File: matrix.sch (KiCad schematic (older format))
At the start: 94 parts, among them SW11 SW_Push, SW12 SW_Push, SW13 SW_Push, SW14 SW_Push, SW16 SW_Push, SW17 SW_Push, SW18 SW_Push, SW2 SW_Push, SW20 SW_Push, SW21 SW_Push, SW22 SW_Push, SW23 SW_Push, SW25 SW_Push, SW26 SW_Push, SW27 SW_Push, SW28 SW_Push, SW3 SW_Push, SW30 SW_Push, SW31 SW_Push, SW32 SW_Push, SW34 SW_Push, SW35 SW_Push, SW36 SW_Push, SW37 SW_Push, SW39 SW_Push, SW4 SW_Push, SW40 SW_Push, SW41 SW_Push, SW43 SW_Push, SW44 SW_Push, SW45 SW_Push, SW46 SW_Push, SW48 SW_Push, SW49 SW_Push, SW5 SW_Push, SW50 SW_Push, SW52 SW_Push, SW53 SW_Push, SW54 SW_Push, SW56 SW_Push, SW57 SW_Push, SW58 SW_Push, SW61 SW_Push, SW62 SW_Push, SW7 SW_Push, SW8 SW_Push, SW9 SW_Push

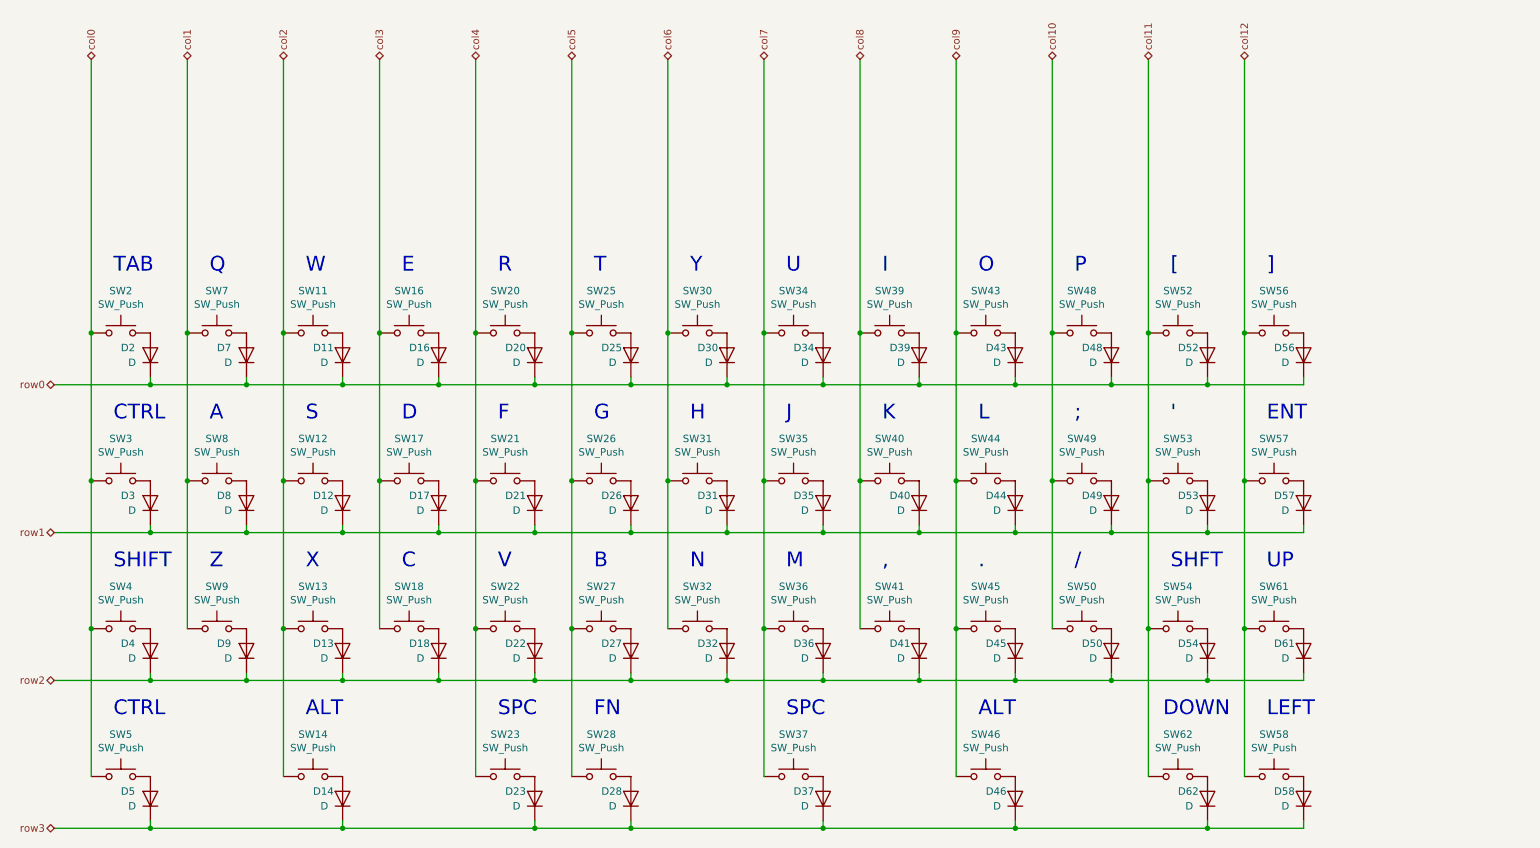
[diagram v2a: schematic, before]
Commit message: Make 69 spacebar layout lol.
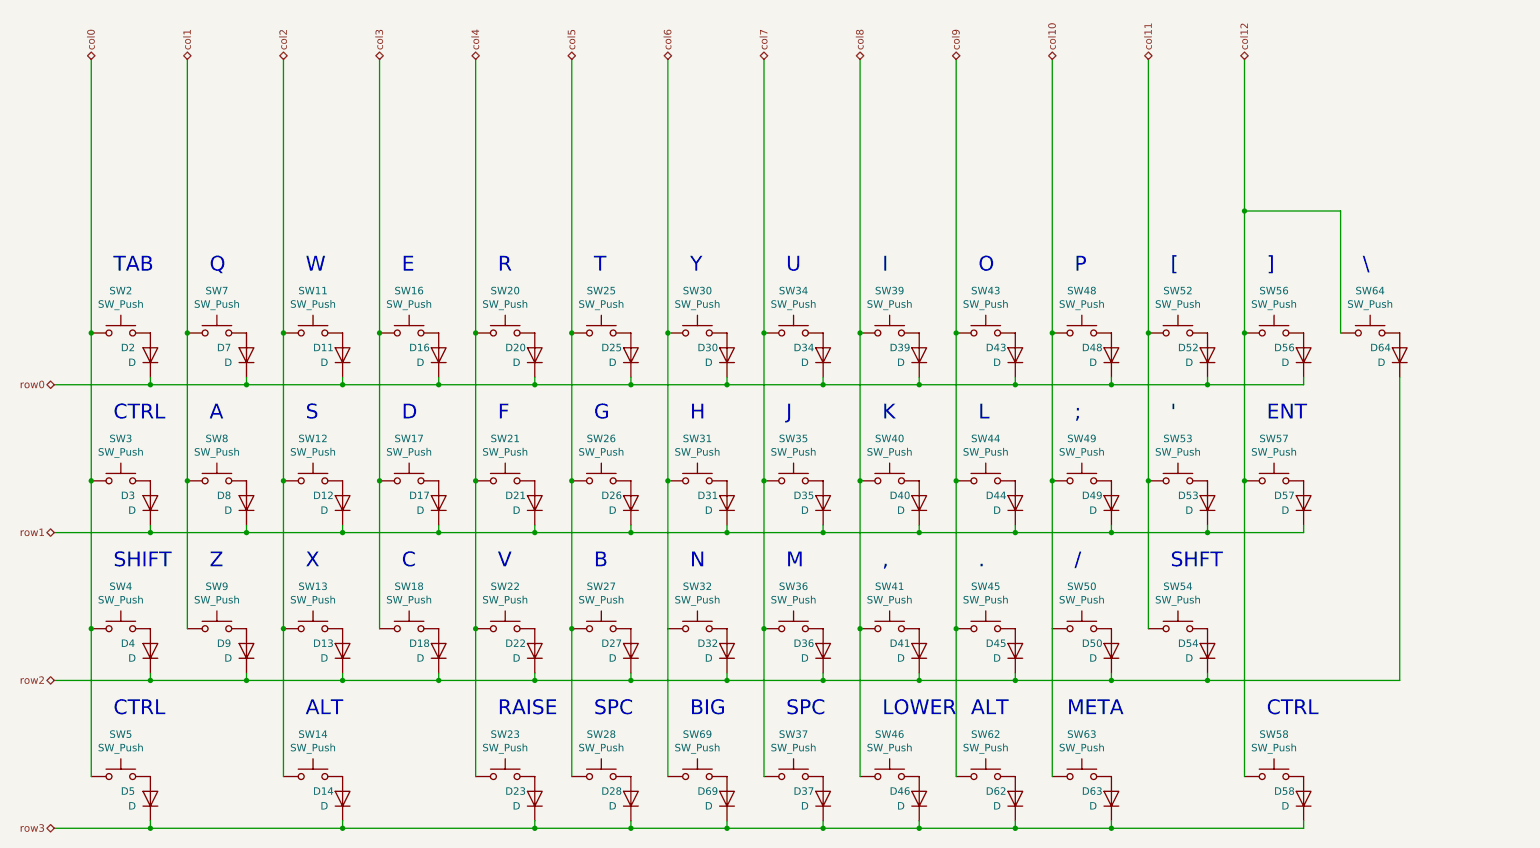
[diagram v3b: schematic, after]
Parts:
- removed D61: D, Diodes_SMD:D_SOD-123, symbol Device:D
- removed SW61: SW_Push, Fate_Parts:SW_Cherry_MX_1.00u_PCB, symbol Switch:SW_Push
- added D63, D64, D69: D, Diode_SMD:D_SOD-123, symbol Device:D
- added SW63, SW64: SW_Push, MX_Switch:SW_Cherry_MX_1.00u_PCB, symbol Switch:SW_Push
- added SW69: SW_Push, Button_Switch_Keyboard:SW_Cherry_MX_6.25u_PCB, symbol Switch:SW_Push
- SW11, SW12, SW13, SW16, SW17, SW18, SW20, SW21, SW22, SW25, SW26, SW27, SW30, SW31, SW32, SW34, SW35, SW36, SW39, SW40, SW41, SW43, SW44, SW45, SW48, SW49, SW50, SW52, SW53, SW56, SW7, SW8, SW9: footprint Fate_Parts:SW_Cherry_MX_1.00u_PCB -> MX_Switch:SW_Cherry_MX_1.00u_PCB
- SW14, SW2, SW46, SW5: footprint Fate_Parts:SW_Cherry_MX_1.50u_PCB -> MX_Switch:SW_Cherry_MX_1.50u_PCB
- SW23: footprint Fate_Parts:SW_Cherry_MX_2.00u_PCB_ReversedStabilizers -> MX_Switch:SW_Cherry_MX_1.00u_PCB
- SW28: footprint Fate_Parts:SW_Cherry_MX_1.00u_PCB -> MX_Switch:SW_Cherry_MX_2.25u_PCB_ReversedStabilizers
- SW3: footprint Fate_Parts:SW_Cherry_MX_1.75u_PCB -> MX_Switch:SW_Cherry_MX_1.75u_PCB
- SW37: footprint Fate_Parts:SW_Cherry_MX_2.75u_PCB_ReversedStabilizers -> MX_Switch:SW_Cherry_MX_2.25u_PCB_ReversedStabilizers
- SW4: footprint Fate_Parts:SW_Cherry_MX_2.25u_PCB -> MX_Switch:SW_Cherry_MX_2.25u_PCB
- SW54: footprint Fate_Parts:SW_Cherry_MX_1.75u_PCB -> MX_Switch:SW_Cherry_MX_2.75u_PCB
- SW57: footprint Fate_Parts:SW_Cherry_MX_2.25u_PCB_ReversedStabilizers -> MX_Switch:SW_Cherry_MX_2.25u_PCB_ReversedStabilizers
- SW58, SW62: footprint Fate_Parts:SW_Cherry_MX_1.00u_PCB -> MX_Switch:SW_Cherry_MX_1.50u_PCB
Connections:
- net col10: now also SW63.1
- net col11: no longer SW62.1
- net col12: now also SW64.1
- net col6: now also SW69.1
- net col8: now also SW46.1
- net col9: now also SW62.1; no longer SW46.1
- net row2: now also D64.1 (K)
- net row3: now also D63.1 (K), D69.1 (K)
- new net: D69.2 (A), SW69.2
- new net: D63.2 (A), SW63.2
- new net: D64.2 (A), SW64.2
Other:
- note added: "BIG"
- note added: "LOWER"
- note added: "META"
- note added: "RAISE"
- note added: "\"
- note removed: "DOWN"
- note removed: "FN"
- note removed: "LEFT"
- note removed: "UP"
- moved on the sheet: D46, D62, SW46, SW62

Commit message: Make it even MORE symmetrical!
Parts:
- removed D69: D, Diode_SMD:D_SOD-123, symbol Device:D
- removed SW69: SW_Push, Button_Switch_Keyboard:SW_Cherry_MX_6.25u_PCB, symbol Switch:SW_Push
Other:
- note removed: "BIG"
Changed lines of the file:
@@
 CTRL
-Wire Wire Line
-	4850 5950 5500 5950
 Wire Wire Line
 	2900 5950 4200 5950
@@
 	7050 4600 7050 5600
 Wire Wire Line
-	5100 4600 5100 5600
-$Comp
-L Switch:SW_Push SW69
-U 1 1 5D407DDB
-P 5300 5600
-F 0 "SW69" H 5300 5885 50  0000 C CNN
-F 1 "SW_Push" H 5300 5794 50  0000 C CNN
-F 2 "Button_Switch_Keyboard:SW_Cherry_MX_6.25u_PCB" H 5300 5800 50  0001 C CNN
-F 3 "" H 5300 5800 50  0001 C CNN
-	1    5300 5600
-	1    0    0    -1
-$EndComp
-$Comp
-L Device:D D69
-U 1 1 5D407DE1
-P 5500 5750
-F 0 "D69" V 5550 5950 50  0000 R CNN
-F 1 "D" V 5450 5900 50  0000 R CNN
-F 2 "Diode_SMD:D_SOD-123" H 5500 5750 50  0001 C CNN
-F 3 "~" H 5500 5750 50  0001 C CNN
-	1    5500 5750
-	0    -1   -1   0
-$EndComp
-Wire Wire Line
-	5500 5900 5500 5950
-Text Notes 5250 5200 0    100  ~ 0
-BIG
-Wire Wire Line
 	9000 3600 9000 5600
-Connection ~ 5500 5950
-Wire Wire Line
-	5500 5950 6150 5950
 Wire Wire Line
 	6400 4600 6400 5600
@@
 	10050 4950 10050 2900
 Connection ~ 8750 4950
+Wire Wire Line
+	4850 5950 6150 5950
 $EndSCHEMATC

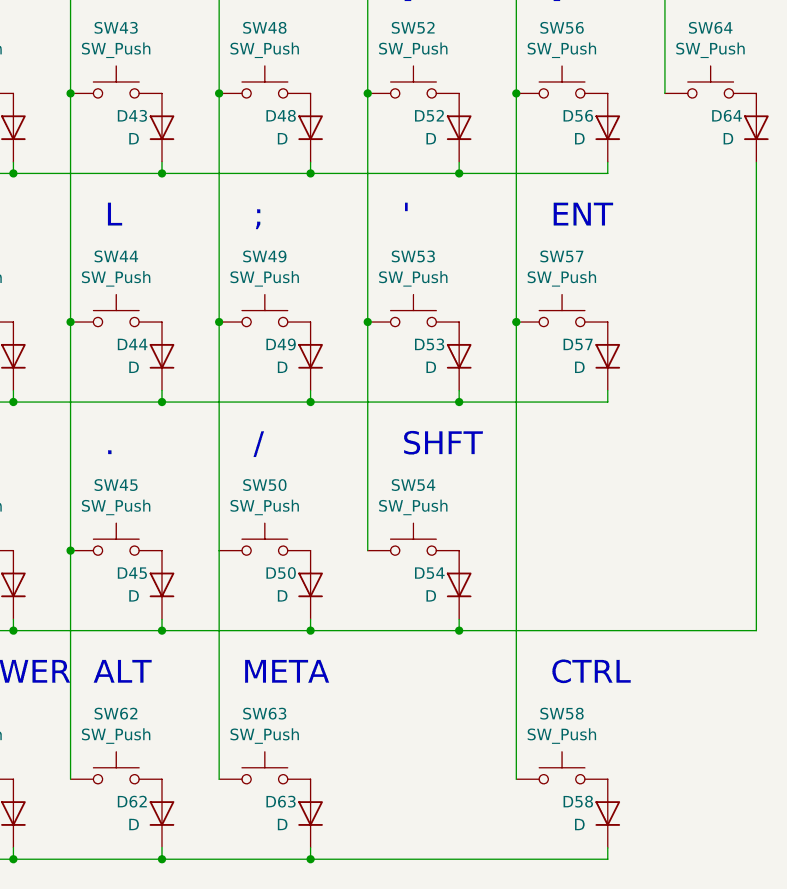
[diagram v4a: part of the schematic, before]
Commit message: Make ergo layout.
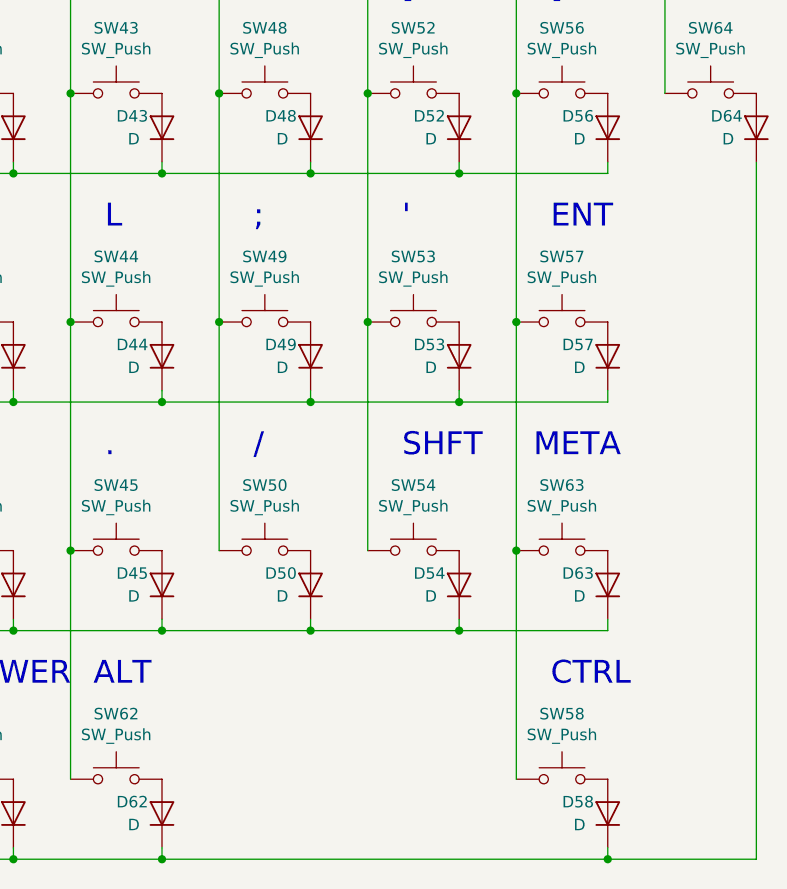
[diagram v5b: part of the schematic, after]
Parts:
- SW28: footprint MX_Switch:SW_Cherry_MX_2.25u_PCB_ReversedStabilizers -> MX_Switch:SW_Cherry_MX_2.00u_PCB_ReversedStabilizers
- SW37: footprint MX_Switch:SW_Cherry_MX_2.25u_PCB_ReversedStabilizers -> MX_Switch:SW_Cherry_MX_2.75u_PCB_ReversedStabilizers
- SW46: footprint MX_Switch:SW_Cherry_MX_1.50u_PCB -> MX_Switch:SW_Cherry_MX_1.00u_PCB
- SW54: footprint MX_Switch:SW_Cherry_MX_2.75u_PCB -> MX_Switch:SW_Cherry_MX_1.75u_PCB
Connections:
- net col10: no longer SW63.1
- net col12: now also SW63.1
- net row2: now also D63.1 (K); no longer D64.1 (K)
- net row3: now also D64.1 (K); no longer D63.1 (K)
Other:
- moved on the sheet: D63, SW63
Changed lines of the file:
@@
 F 0 "SW28" H 4650 5885 50  0000 C CNN
 F 1 "SW_Push" H 4650 5794 50  0000 C CNN
-F 2 "MX_Switch:SW_Cherry_MX_2.25u_PCB_ReversedStabilizers" H 4650 5800 50  0001 C CNN
+F 2 "MX_Switch:SW_Cherry_MX_2.00u_PCB_ReversedStabilizers" H 4650 5800 50  0001 C CNN
 F 3 "" H 4650 5800 50  0001 C CNN
 	1    4650 5600
@@
 F 0 "SW37" H 5950 5885 50  0000 C CNN
 F 1 "SW_Push" H 5950 5794 50  0000 C CNN
-F 2 "MX_Switch:SW_Cherry_MX_2.25u_PCB_ReversedStabilizers" H 5950 5800 50  0001 C CNN
+F 2 "MX_Switch:SW_Cherry_MX_2.75u_PCB_ReversedStabilizers" H 5950 5800 50  0001 C CNN
 F 3 "" H 5950 5800 50  0001 C CNN
 	1    5950 5600
@@
 F 0 "SW54" H 8550 4885 50  0000 C CNN
 F 1 "SW_Push" H 8550 4794 50  0000 C CNN
-F 2 "MX_Switch:SW_Cherry_MX_2.75u_PCB" H 8550 4800 50  0001 C CNN
+F 2 "MX_Switch:SW_Cherry_MX_1.75u_PCB" H 8550 4800 50  0001 C CNN
 F 3 "" H 8550 4800 50  0001 C CNN
 	1    8550 4600
@@
 	7050 4600 7050 5600
 Wire Wire Line
-	9000 3600 9000 5600
+	9000 3600 9000 4600
 Wire Wire Line
 	6400 4600 6400 5600
@@
 F 0 "SW46" H 6600 5885 50  0000 C CNN
 F 1 "SW_Push" H 6600 5794 50  0000 C CNN
-F 2 "MX_Switch:SW_Cherry_MX_1.50u_PCB" H 6600 5800 50  0001 C CNN
+F 2 "MX_Switch:SW_Cherry_MX_1.00u_PCB" H 6600 5800 50  0001 C CNN
 F 3 "" H 6600 5800 50  0001 C CNN
 	1    6600 5600
@@
 	7450 5900 7450 5950
 Connection ~ 7450 5950
-Wire Wire Line
-	7450 5950 8100 5950
 $Comp
 L Switch:SW_Push SW63
 U 1 1 5D4A7C9A
-P 7900 5600
-F 0 "SW63" H 7900 5885 50  0000 C CNN
-F 1 "SW_Push" H 7900 5794 50  0000 C CNN
-F 2 "MX_Switch:SW_Cherry_MX_1.00u_PCB" H 7900 5800 50  0001 C CNN
-F 3 "" H 7900 5800 50  0001 C CNN
-	1    7900 5600
+P 9200 4600
+F 0 "SW63" H 9200 4885 50  0000 C CNN
+F 1 "SW_Push" H 9200 4794 50  0000 C CNN
+F 2 "MX_Switch:SW_Cherry_MX_1.00u_PCB" H 9200 4800 50  0001 C CNN
+F 3 "" H 9200 4800 50  0001 C CNN
+	1    9200 4600
 	1    0    0    -1
 $EndComp
@@
 L Device:D D63
 U 1 1 5D4A7CA0
-P 8100 5750
-F 0 "D63" V 8150 5950 50  0000 R CNN
-F 1 "D" V 8050 5900 50  0000 R CNN
-F 2 "Diode_SMD:D_SOD-123" H 8100 5750 50  0001 C CNN
-F 3 "~" H 8100 5750 50  0001 C CNN
-	1    8100 5750
-	0    -1   -1   0
-$EndComp
-Text Notes 7800 5200 0    100  ~ 0
+P 9400 4750
+F 0 "D63" V 9450 4950 50  0000 R CNN
+F 1 "D" V 9350 4900 50  0000 R CNN
+F 2 "Diode_SMD:D_SOD-123" H 9400 4750 50  0001 C CNN
+F 3 "~" H 9400 4750 50  0001 C CNN
+	1    9400 4750
+	0    -1   -1   0
+$EndComp
+Text Notes 9075 4200 0    100  ~ 0
 META
-Wire Wire Line
-	7700 4600 7700 5600
-Wire Wire Line
-	8100 5900 8100 5950
-Connection ~ 8100 5950
-Wire Wire Line
-	8100 5950 9400 5950
 $Comp
 L Switch:SW_Push SW64
@@
 	9000 1775 9000 2600
 Wire Wire Line
-	8750 4950 10050 4950
-Wire Wire Line
-	10050 4950 10050 2900
+	4850 5950 6150 5950
+Wire Wire Line
+	9400 5950 10050 5950
+Connection ~ 9400 5950
+Wire Wire Line
+	10050 2900 10050 5950
+Connection ~ 9000 4600
+Wire Wire Line
+	9000 4600 9000 5600
+Wire Wire Line
+	7450 5950 9400 5950
+Wire Wire Line
+	8750 4950 9400 4950
+Wire Wire Line
+	9400 4950 9400 4900
 Connection ~ 8750 4950
-Wire Wire Line
-	4850 5950 6150 5950
 $EndSCHEMATC

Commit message: Route more traces.
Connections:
- net col11: now also SW64.1
- net col12: no longer SW64.1
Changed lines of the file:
@@
 	7700 750  7700 2600
 Wire Wire Line
-	8350 750  8350 2600
-Wire Wire Line
-	9000 750  9000 1775
+	8350 750  8350 1775
 Text HLabel 1200 750  1    50   3State ~ 0
 col0
@@
 \
 Wire Wire Line
-	9000 1775 9650 1775
-Wire Wire Line
 	9650 1775 9650 2600
-Connection ~ 9000 1775
-Wire Wire Line
-	9000 1775 9000 2600
 Wire Wire Line
 	4850 5950 6150 5950
@@
 	9400 4950 9400 4900
 Connection ~ 8750 4950
+Wire Wire Line
+	9000 1775 8350 1775
+Connection ~ 8350 1775
+Wire Wire Line
+	8350 1775 8350 2600
+Wire Wire Line
+	9000 750  9000 2600
+Wire Wire Line
+	9000 1775 9650 1775
 $EndSCHEMATC

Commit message: Finalize PCB design for round 1.
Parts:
- removed D64: D, Diode_SMD:D_SOD-123, symbol Device:D
- removed SW64: SW_Push, MX_Switch:SW_Cherry_MX_1.00u_PCB, symbol Switch:SW_Push
- SW57: footprint MX_Switch:SW_Cherry_MX_2.25u_PCB_ReversedStabilizers -> MX_Switch:SW_Cherry_MX_1.75u_PCB
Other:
- note removed: "\"
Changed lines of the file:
@@
 F 0 "SW57" H 9200 3885 50  0000 C CNN
 F 1 "SW_Push" H 9200 3794 50  0000 C CNN
-F 2 "MX_Switch:SW_Cherry_MX_2.25u_PCB_ReversedStabilizers" H 9200 3800 50  0001 C CNN
+F 2 "MX_Switch:SW_Cherry_MX_1.75u_PCB" H 9200 3800 50  0001 C CNN
 F 3 "" H 9200 3800 50  0001 C CNN
 	1    9200 3600
@@
 Wire Wire Line
 	7700 750  7700 2600
-Wire Wire Line
-	8350 750  8350 1775
 Text HLabel 1200 750  1    50   3State ~ 0
 col0
@@
 Text Notes 9075 4200 0    100  ~ 0
 META
-$Comp
-L Switch:SW_Push SW64
-U 1 1 5D4B4965
-P 9850 2600
-F 0 "SW64" H 9850 2885 50  0000 C CNN
-F 1 "SW_Push" H 9850 2794 50  0000 C CNN
-F 2 "MX_Switch:SW_Cherry_MX_1.00u_PCB" H 9850 2800 50  0001 C CNN
-F 3 "" H 9850 2800 50  0001 C CNN
-	1    9850 2600
-	1    0    0    -1
-$EndComp
-$Comp
-L Device:D D64
-U 1 1 5D4B496B
-P 10050 2750
-F 0 "D64" V 10100 2950 50  0000 R CNN
-F 1 "D" V 10000 2900 50  0000 R CNN
-F 2 "Diode_SMD:D_SOD-123" H 10050 2750 50  0001 C CNN
-F 3 "~" H 10050 2750 50  0001 C CNN
-	1    10050 2750
-	0    -1   -1   0
-$EndComp
-Text Notes 9800 2200 0    100  ~ 0
-\
-Wire Wire Line
-	9650 1775 9650 2600
 Wire Wire Line
 	4850 5950 6150 5950
-Wire Wire Line
-	9400 5950 10050 5950
-Connection ~ 9400 5950
-Wire Wire Line
-	10050 2900 10050 5950
 Connection ~ 9000 4600
 Wire Wire Line
@@
 Connection ~ 8750 4950
 Wire Wire Line
-	9000 1775 8350 1775
-Connection ~ 8350 1775
-Wire Wire Line
-	8350 1775 8350 2600
-Wire Wire Line
 	9000 750  9000 2600
 Wire Wire Line
-	9000 1775 9650 1775
+	8350 750  8350 2600
 $EndSCHEMATC
